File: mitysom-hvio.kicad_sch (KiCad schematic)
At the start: 1 part, among them J100 Plug_Samtec_SEAM-50-02.0-L-08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

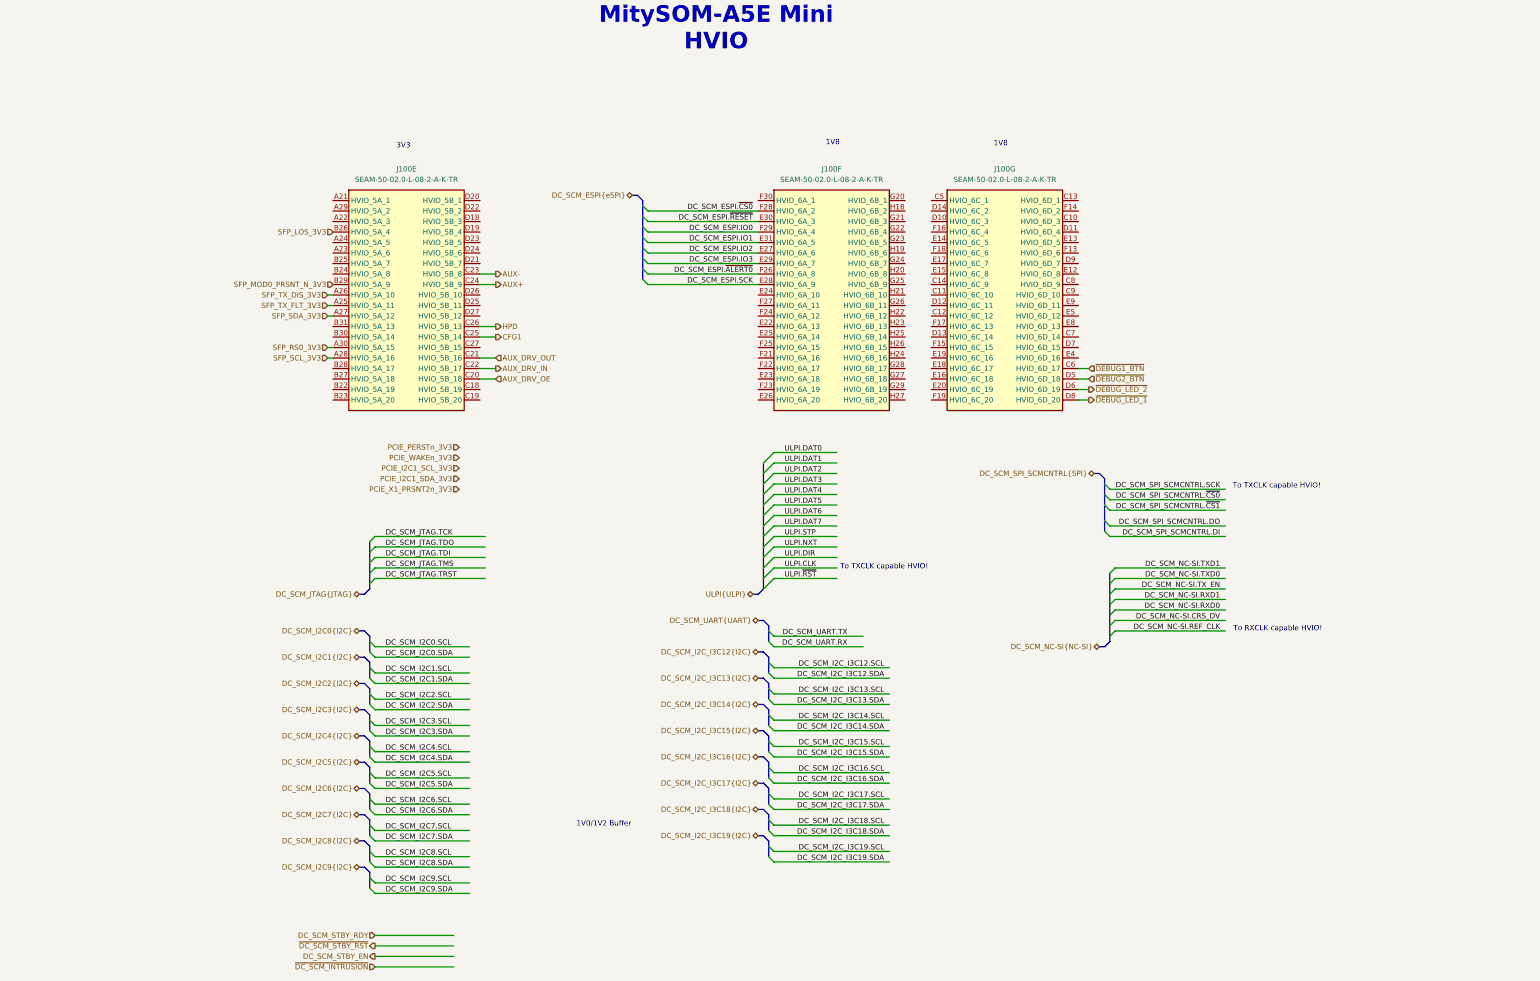
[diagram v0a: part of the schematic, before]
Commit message: [#100282] Connect signals to HVIO banks
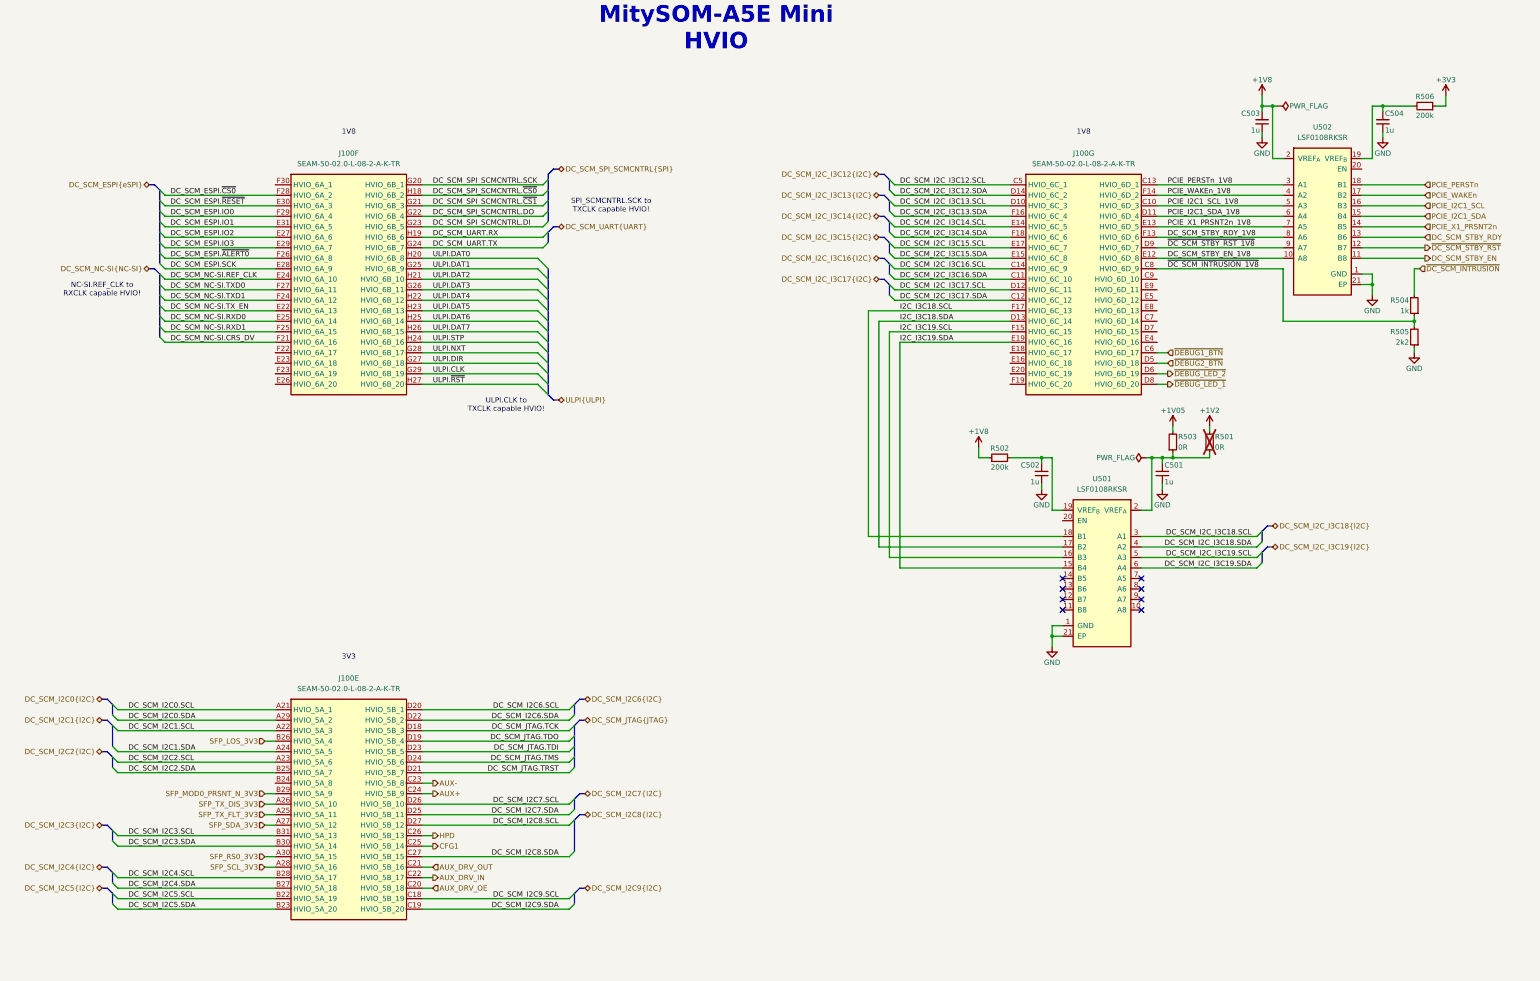
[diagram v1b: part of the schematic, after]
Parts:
- added C501, C502, C503, C504: C_1u_0402, antmicro-footprints:C_0402_1005Metric, symbol antmicroCapacitors0402:C_1u_0402
- added R501, R503: R_0R_0402, antmicro-footprints:R_0402_1005Metric, symbol antmicroResistors0402:R_0R_0402
- added R502, R506: R_200k_0402, antmicro-footprints:R_0402_1005Metric, symbol antmicroResistors0402:R_200k_0402
- added R504: R_1k_0402, antmicro-footprints:R_0402_1005Metric, symbol antmicroResistors0402:R_1k_0402
- added R505: R_2k2_0402, antmicro-footprints:R_0402_1005Metric, symbol antmicroResistors0402:R_2k2_0402
- added U501, U502: LSF0108RKSR, antmicro-footprints:VQFN-20_1EP_4.5x2.5mm_P0.5mm, symbol antmicroLogicTranslatorsLevelShifters:LSF0108RKSR
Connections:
- net DC_SCM_I2C0.SCL: now also J100.A21 (HVIO_5A_1)
- net DC_SCM_I2C0.SDA: now also J100.A29 (HVIO_5A_2)
- net DC_SCM_I2C1.SCL: now also J100.A22 (HVIO_5A_3)
- net DC_SCM_I2C1.SDA: now also J100.A24 (HVIO_5A_5)
- net DC_SCM_I2C2.SCL: now also J100.A23 (HVIO_5A_6)
- net DC_SCM_I2C2.SDA: now also J100.B25 (HVIO_5A_7)
- net DC_SCM_I2C3.SCL: now also J100.B31 (HVIO_5A_13)
- net DC_SCM_I2C3.SDA: now also J100.B30 (HVIO_5A_14)
- net DC_SCM_I2C4.SCL: now also J100.B28 (HVIO_5A_17)
- net DC_SCM_I2C4.SDA: now also J100.B27 (HVIO_5A_18)
- net DC_SCM_I2C5.SCL: now also J100.B22 (HVIO_5A_19)
- net DC_SCM_I2C5.SDA: now also J100.B23 (HVIO_5A_20)
- net DC_SCM_I2C6.SCL: now also J100.D20 (HVIO_5B_1)
- net DC_SCM_I2C6.SDA: now also J100.D22 (HVIO_5B_2)
- net DC_SCM_I2C7.SCL: now also J100.D26 (HVIO_5B_10)
- net DC_SCM_I2C7.SDA: now also J100.D25 (HVIO_5B_11)
- net DC_SCM_I2C8.SCL: now also J100.D27 (HVIO_5B_12)
- net DC_SCM_I2C8.SDA: now also J100.C27 (HVIO_5B_15)
- net DC_SCM_I2C9.SCL: now also J100.C18 (HVIO_5B_19)
- net DC_SCM_I2C9.SDA: now also J100.C19 (HVIO_5B_20)
- net DC_SCM_I2C_I3C12.SCL: now also J100.C5 (HVIO_6C_1)
- net DC_SCM_I2C_I3C12.SDA: now also J100.D14 (HVIO_6C_2)
- net DC_SCM_I2C_I3C13.SCL: now also J100.D10 (HVIO_6C_3)
- net DC_SCM_I2C_I3C13.SDA: now also J100.F16 (HVIO_6C_4)
- net DC_SCM_I2C_I3C14.SCL: now also J100.E14 (HVIO_6C_5)
- net DC_SCM_I2C_I3C14.SDA: now also J100.F18 (HVIO_6C_6)
- net DC_SCM_I2C_I3C15.SCL: now also J100.E17 (HVIO_6C_7)
- net DC_SCM_I2C_I3C15.SDA: now also J100.E15 (HVIO_6C_8)
- net DC_SCM_I2C_I3C16.SCL: now also J100.C14 (HVIO_6C_9)
- net DC_SCM_I2C_I3C16.SDA: now also J100.C11 (HVIO_6C_10)
- net DC_SCM_I2C_I3C17.SCL: now also J100.D12 (HVIO_6C_11)
- net DC_SCM_I2C_I3C17.SDA: now also J100.C12 (HVIO_6C_12)
- net DC_SCM_I2C_I3C18.SCL: now also U501.3 (A1)
- net DC_SCM_I2C_I3C18.SDA: now also U501.4 (A2)
- net DC_SCM_I2C_I3C19.SCL: now also U501.5 (A3)
- net DC_SCM_I2C_I3C19.SDA: now also U501.6 (A4)
- net DC_SCM_JTAG.TCK: now also J100.D18 (HVIO_5B_3)
- net DC_SCM_JTAG.TDI: now also J100.D23 (HVIO_5B_5)
- net DC_SCM_JTAG.TDO: now also J100.D19 (HVIO_5B_4)
- net DC_SCM_JTAG.TMS: now also J100.D24 (HVIO_5B_6)
- net DC_SCM_JTAG.TRST: now also J100.D21 (HVIO_5B_7)
- net DC_SCM_NC-SI.CRS_DV: now also J100.F21 (HVIO_6A_16)
- net DC_SCM_NC-SI.REF_CLK: now also J100.E24 (HVIO_6A_10)
- net DC_SCM_NC-SI.RXD0: now also J100.E25 (HVIO_6A_14)
- net DC_SCM_NC-SI.RXD1: now also J100.F25 (HVIO_6A_15)
- net DC_SCM_NC-SI.TXD0: now also J100.F27 (HVIO_6A_11)
- net DC_SCM_NC-SI.TXD1: now also J100.F24 (HVIO_6A_12)
- net DC_SCM_NC-SI.TX_EN: now also J100.E22 (HVIO_6A_13)
- net DC_SCM_SPI_SCMCNTRL.DI: now also J100.G23 (HVIO_6B_5)
- net DC_SCM_SPI_SCMCNTRL.DO: now also J100.G22 (HVIO_6B_4)
- net DC_SCM_SPI_SCMCNTRL.SCK: now also J100.G20 (HVIO_6B_1)
- net DC_SCM_SPI_SCMCNTRL.~{CS0}: now also J100.H18 (HVIO_6B_2)
- net DC_SCM_SPI_SCMCNTRL.~{CS1}: now also J100.G21 (HVIO_6B_3)
- net DC_SCM_STBY_EN: now also U502.11 (B8)
- net DC_SCM_STBY_RDY: now also U502.13 (B6)
- net DC_SCM_UART.RX: now also J100.H19 (HVIO_6B_6)
- net DC_SCM_UART.TX: now also J100.G24 (HVIO_6B_7)
- net ULPI.CLK: now also J100.G29 (HVIO_6B_19)
- net ULPI.DAT0: now also J100.H20 (HVIO_6B_8)
- net ULPI.DAT1: now also J100.G25 (HVIO_6B_9)
- net ULPI.DAT2: now also J100.H21 (HVIO_6B_10)
- net ULPI.DAT3: now also J100.G26 (HVIO_6B_11)
- net ULPI.DAT4: now also J100.H22 (HVIO_6B_12)
- net ULPI.DAT5: now also J100.H23 (HVIO_6B_13)
- net ULPI.DAT6: now also J100.H25 (HVIO_6B_14)
- net ULPI.DAT7: now also J100.H26 (HVIO_6B_15)
- net ULPI.DIR: now also J100.G27 (HVIO_6B_18)
- net ULPI.NXT: now also J100.G28 (HVIO_6B_17)
- net ULPI.STP: now also J100.H24 (HVIO_6B_16)
- net ULPI.~{RST}: now also J100.H27 (HVIO_6B_20)
- net ~{DC_SCM_INTRUSION}: now also R504.2
- net ~{DC_SCM_STBY_RST}: now also U502.12 (B7)
- net PCIE_I2C1_SCL_1V8: now reaches J100.C10 (HVIO_6D_3)
- net PCIE_I2C1_SCL_1V8: now also U502.5 (A3)
- net PCIE_PERSTn_1V8: now reaches J100.C13 (HVIO_6D_1)
- net PCIE_PERSTn_1V8: now also U502.3 (A1)
- net ~{DC_SCM_INTRUSION_1V8}: now reaches J100.C8 (HVIO_6D_9)
- net ~{DC_SCM_INTRUSION_1V8}: now also R504.1, R505.2
- net PCIE_I2C1_SDA_1V8: now reaches J100.D11 (HVIO_6D_4)
- net PCIE_I2C1_SDA_1V8: now also U502.6 (A4)
- net I2C_I3C18.SDA: now reaches J100.D13 (HVIO_6C_14)
- net I2C_I3C18.SDA: now also U501.17 (B2)
- net ~{DC_SCM_STBY_RST_1V8}: now reaches J100.D9 (HVIO_6D_7)
- net ~{DC_SCM_STBY_RST_1V8}: now also U502.9 (A7)
- net DC_SCM_STBY_EN_1V8: now reaches J100.E12 (HVIO_6D_8)
- net DC_SCM_STBY_EN_1V8: now also U502.10 (A8)
- net PCIE_X1_PRSNT2n_1V8: now reaches J100.E13 (HVIO_6D_5)
- net PCIE_X1_PRSNT2n_1V8: now also U502.7 (A5)
- net I2C_I3C19.SDA: now reaches J100.E19 (HVIO_6C_16)
- net I2C_I3C19.SDA: now also U501.15 (B4)
- net DC_SCM_STBY_RDY_1V8: now reaches J100.F13 (HVIO_6D_6)
- net DC_SCM_STBY_RDY_1V8: now also U502.8 (A6)
- net PCIE_WAKEn_1V8: now reaches J100.F14 (HVIO_6D_2)
- net PCIE_WAKEn_1V8: now also U502.4 (A2)
- net I2C_I3C19.SCL: now reaches J100.F15 (HVIO_6C_15)
- net I2C_I3C19.SCL: now also U501.16 (B3)
- net I2C_I3C18.SCL: now reaches J100.F17 (HVIO_6C_13)
- net I2C_I3C18.SCL: now also U501.18 (B1)
- new net: C501.2, R501.1, R503.1, U501.2 (VREF_{A})
- new net: C504.2, R506.2, U502.19 (VREF_{B})
- new net: C502.2, R502.2, U501.19 (VREF_{B})
- new net +1V05: R503.2
- new net +1V2: R501.2
- new net +1V8: C503.2, R502.1, U502.2 (VREF_{A})
- new net +3V3: R506.1
- new net GND: C501.1, C502.1, C503.1, C504.1, R505.1, U501.1 (GND), U501.21 (EP), U502.1 (GND), U502.21 (EP)
- new net PCIE_I2C1_SCL: U502.16 (B3)
- new net PCIE_I2C1_SDA: U502.15 (B4)
- new net PCIE_PERSTn: U502.18 (B1)
- new net PCIE_WAKEn: U502.17 (B2)
- new net PCIE_X1_PRSNT2n: U502.14 (B5)
- no-connect marks 0 -> 8
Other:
- note added: "NC-SI.REF_CLK to RXCLK capable HVIO!"
- note added: "SPI_SCMCNTRL.SCK to TXCLK capable HVIO!"
- note added: "ULPI.CLK to TXCLK capable HVIO!"
- note removed: "1V0/1V2 Buffer"
- note removed: "To RXCLK capable HVIO!"
- note removed: "To TXCLK capable HVIO!"
- moved on the sheet: J100E, J100F, J100G

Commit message: [#100282] Swap TMP default from QSPI to SPI, add level shifter for PECI I2C bus, connect user button
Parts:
- removed R501: R_0R_0402, antmicro-footprints:R_0402_1005Metric, symbol antmicroResistors0402:R_0R_0402
- removed R502: R_200k_0402, antmicro-footprints:R_0402_1005Metric, symbol antmicroResistors0402:R_200k_0402
- added R501: R_200k_0402, antmicro-footprints:R_0402_1005Metric, symbol antmicroResistors0402:R_200k_0402
- added R502: R_0R_0402, antmicro-footprints:R_0402_1005Metric, symbol antmicroResistors0402:R_0R_0402
- R503: now not fitted
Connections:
- net +1V05: now also R502.2; no longer R503.2
- net +1V2: now also R503.2
- net +1V8: now also R501.1
- net I2C_I3C18.SCL: now also J100.F22 (HVIO_6A_17); no longer J100.F17 (HVIO_6C_13)
- net I2C_I3C18.SDA: now also J100.E23 (HVIO_6A_18); no longer J100.D13 (HVIO_6C_14)
- net I2C_I3C19.SCL: now also J100.F23 (HVIO_6A_19); no longer J100.F15 (HVIO_6C_15)
- net I2C_I3C19.SDA: now also J100.E26 (HVIO_6A_20); no longer J100.E19 (HVIO_6C_16)
- net at R503.1, U501.2 (VREF_{A}): now also C502.2, R502.1; no longer C501.2
- net at U501.19 (VREF_{B}): now also C501.2, R501.2; no longer C502.2
- net TPM_MUX_SEL: now reaches J100.D7 (HVIO_6D_15)
- net SOM.SCK: now reaches J100.E16 (HVIO_6C_18)
- net SOM.~{CS0}: now reaches J100.E18 (HVIO_6C_17)
- net ~{USER_BTN}: now reaches J100.E4 (HVIO_6D_16)
- new net SOM.IO0: J100.E19 (HVIO_6C_16)
- new net SOM.IO1: J100.F15 (HVIO_6C_15)
- new net SOM.IO2: J100.D13 (HVIO_6C_14)
- new net SOM.IO3: J100.F17 (HVIO_6C_13)
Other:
- moved on the sheet: C503, C504, J100E, J100F, J100G, R504, R505, R506, U502

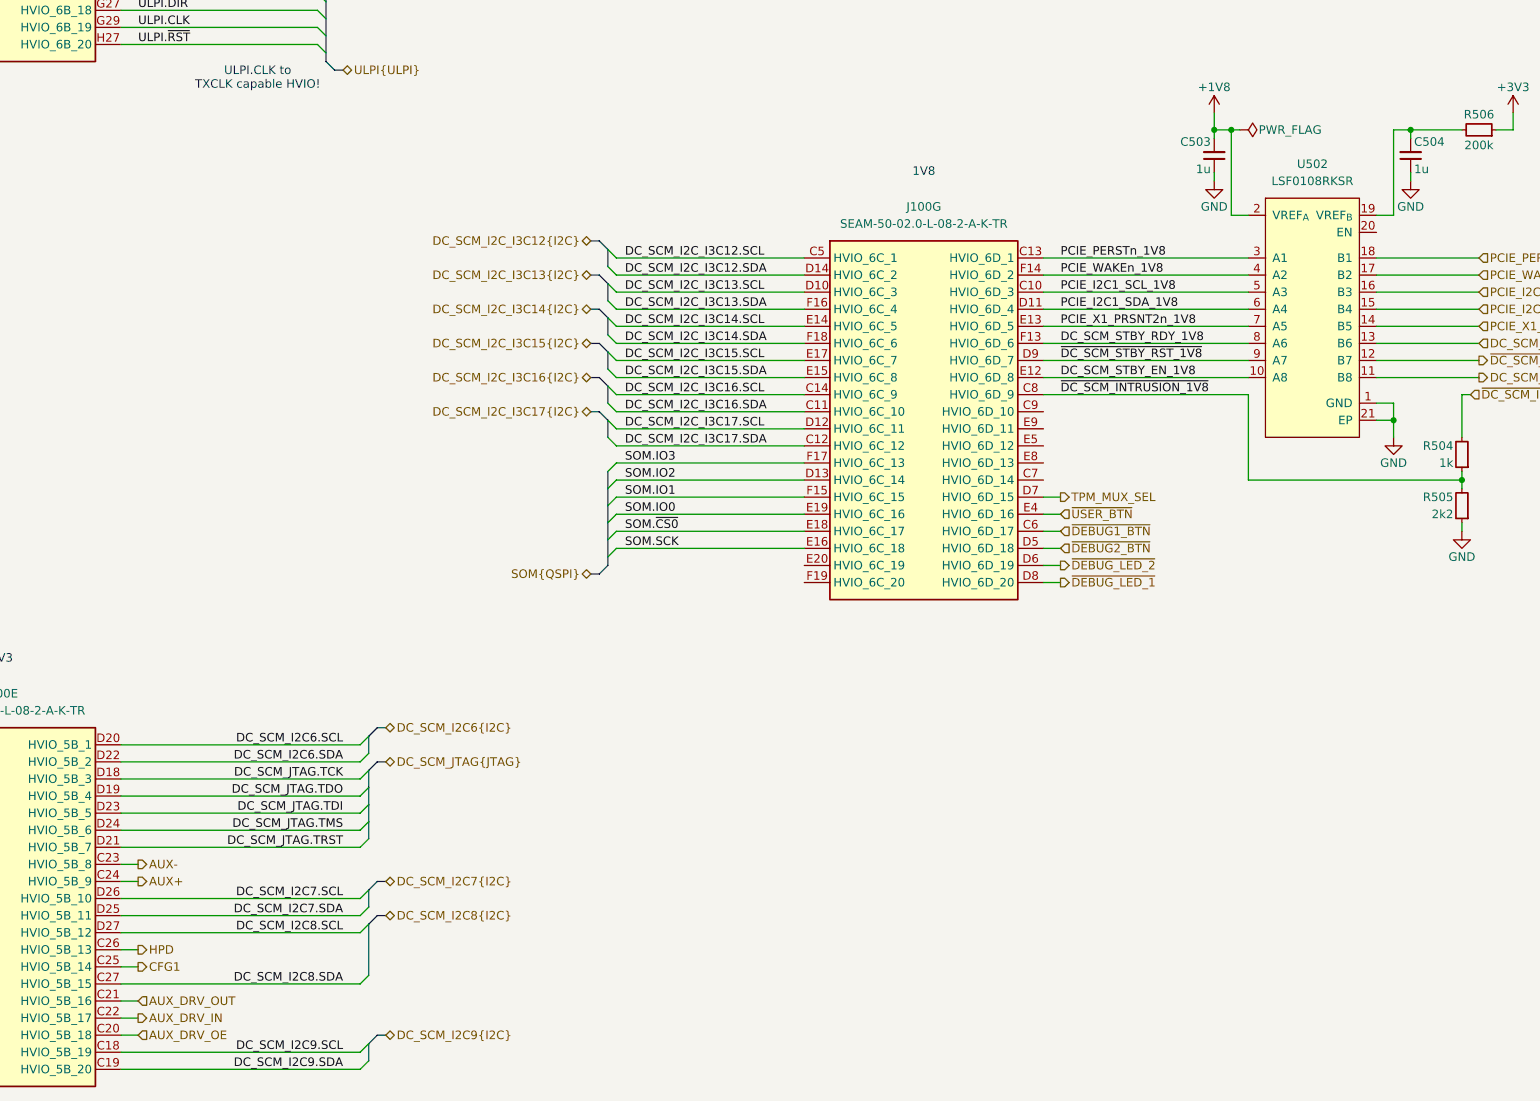
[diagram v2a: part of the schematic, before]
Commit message: [#100282] Move AUX, HPD, CONFIG and AUX_DRV to separate DP_CTRL bus, connect HS connector remaining DP signals
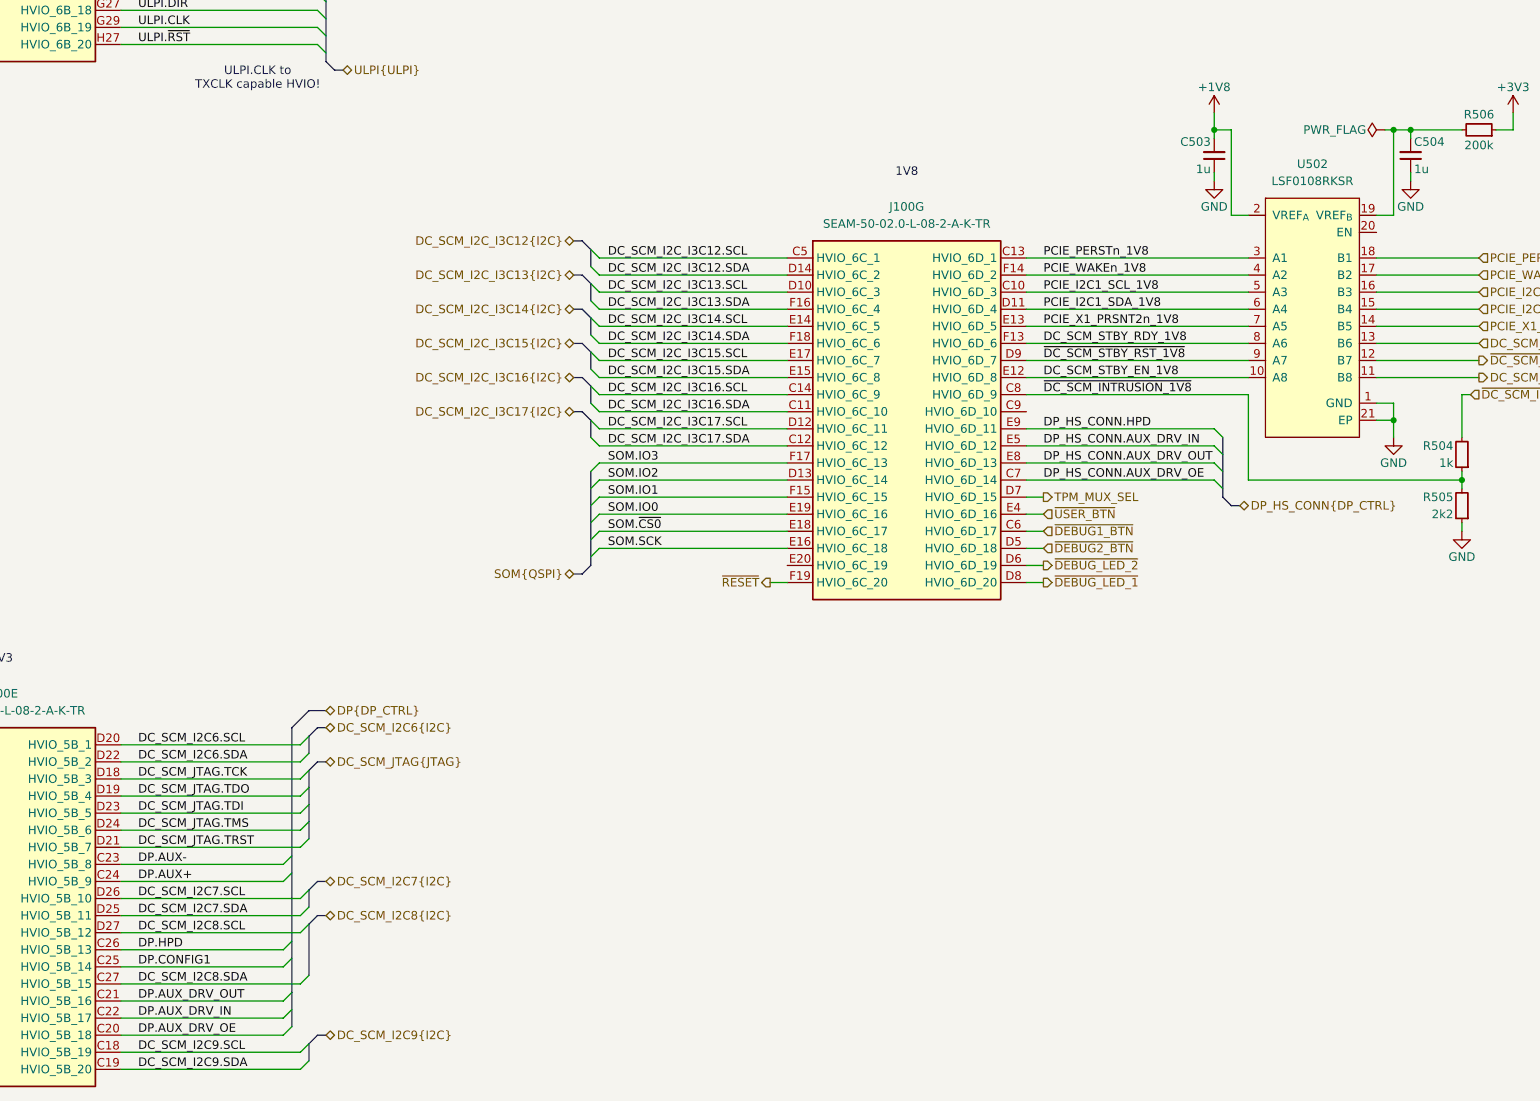
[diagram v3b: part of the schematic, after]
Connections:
- net DP_HS_CONN.AUX_DRV_OE: now reaches J100.C7 (HVIO_6D_14)
- net DP_HS_CONN.AUX_DRV_IN: now reaches J100.E5 (HVIO_6D_12)
- net DP_HS_CONN.AUX_DRV_OUT: now reaches J100.E8 (HVIO_6D_13)
- net DP_HS_CONN.HPD: now reaches J100.E9 (HVIO_6D_11)
- net ~{RESET}: now reaches J100.F19 (HVIO_6C_20)
- net AUX+ renamed DP.AUX+
- net AUX- renamed DP.AUX-
- net AUX_DRV_IN renamed DP.AUX_DRV_IN
- net AUX_DRV_OE renamed DP.AUX_DRV_OE
- net AUX_DRV_OUT renamed DP.AUX_DRV_OUT
- net CFG1 renamed DP.CONFIG1
- net HPD renamed DP.HPD
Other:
- moved on the sheet: J100G
